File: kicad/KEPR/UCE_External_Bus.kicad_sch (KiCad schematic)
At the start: 6 parts, among them J10 Conn_02x40_Odd_Even, J13 PINHD_2x2_Male, J6 Conn_02x20_Odd_Even, J7 Conn_02x08_Odd_Even, J8 Conn_01x08_Pin, J9 Conn_02x40_Odd_Even

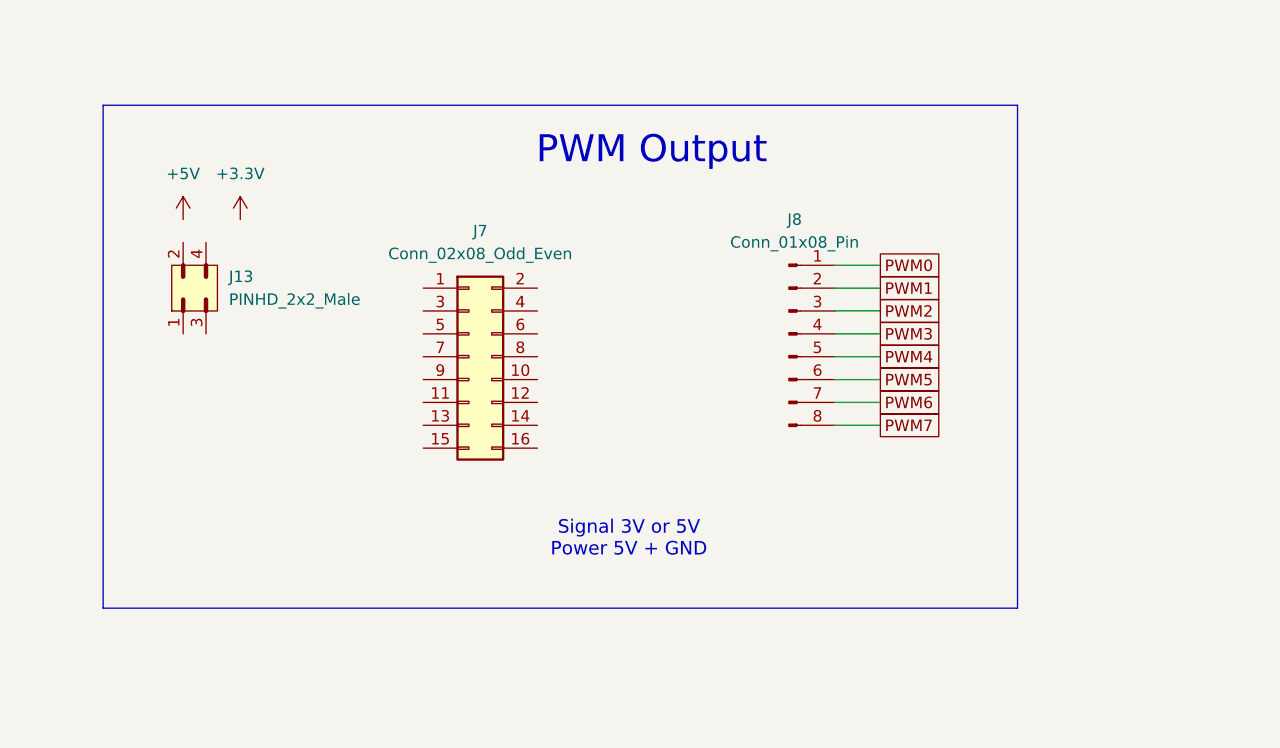
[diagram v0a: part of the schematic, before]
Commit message: Mais trilhas e vias lançadas
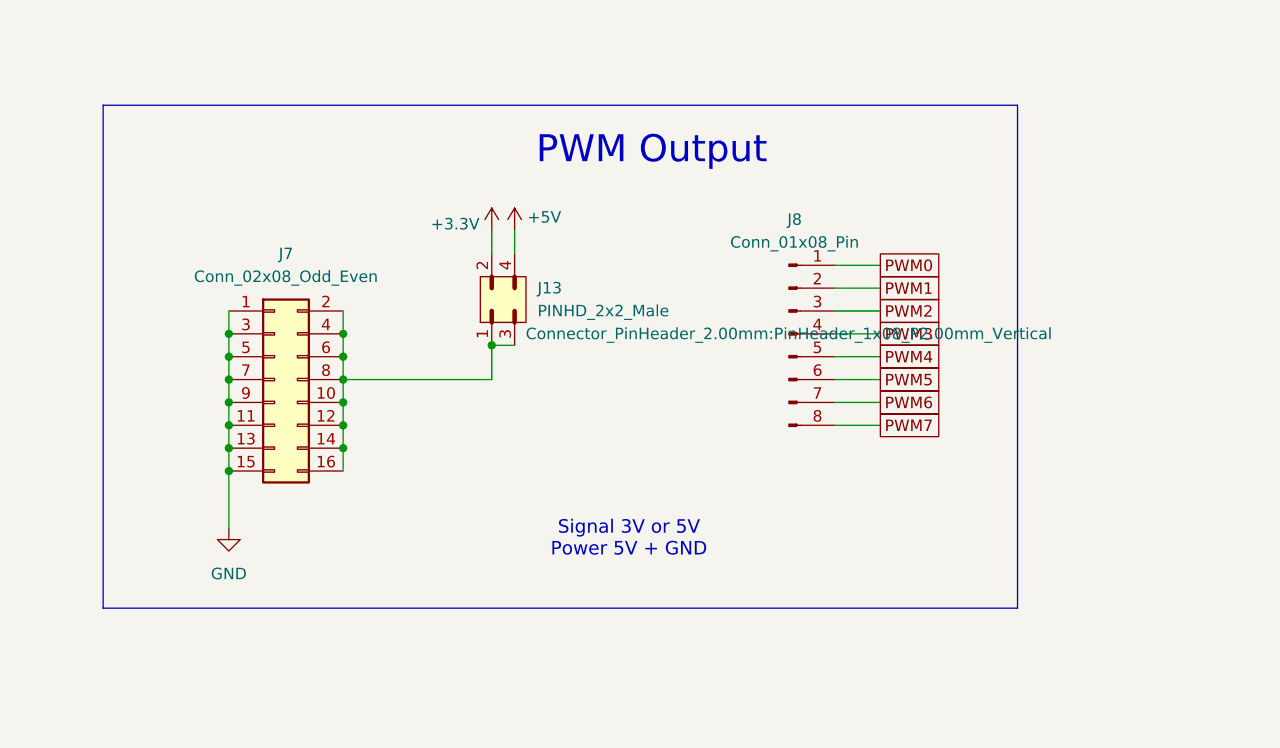
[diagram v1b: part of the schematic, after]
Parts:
- J7: footprint (none) -> Connector_PinHeader_2.00mm:PinHeader_2x08_P2.00mm_Vertical
- J8: footprint (none) -> Connector_PinHeader_2.00mm:PinHeader_1x08_P2.00mm_Vertical
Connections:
- net +3.3V: now also J13.2
- net +5V: now also J13.4
- net GND: now also J7.1 (Pin_1), J7.11 (Pin_11), J7.13 (Pin_13), J7.15 (Pin_15), J7.3 (Pin_3), J7.5 (Pin_5), J7.7 (Pin_7), J7.9 (Pin_9)
- net at J7.10 (Pin_10): now also J13.1, J13.3, J7.12 (Pin_12), J7.14 (Pin_14), J7.16 (Pin_16), J7.2 (Pin_2), J7.4 (Pin_4), J7.6 (Pin_6), J7.8 (Pin_8)
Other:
- moved on the sheet: J13, J7
